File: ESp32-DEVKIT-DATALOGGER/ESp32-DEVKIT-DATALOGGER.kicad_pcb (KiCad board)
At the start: 2 copper layers, 9 parts, among them J1 Socket_01x02, J2 Conn_01x04, SW1 SW_Omron_B3FS, U1 ESP32-S3-MINI-1-N8

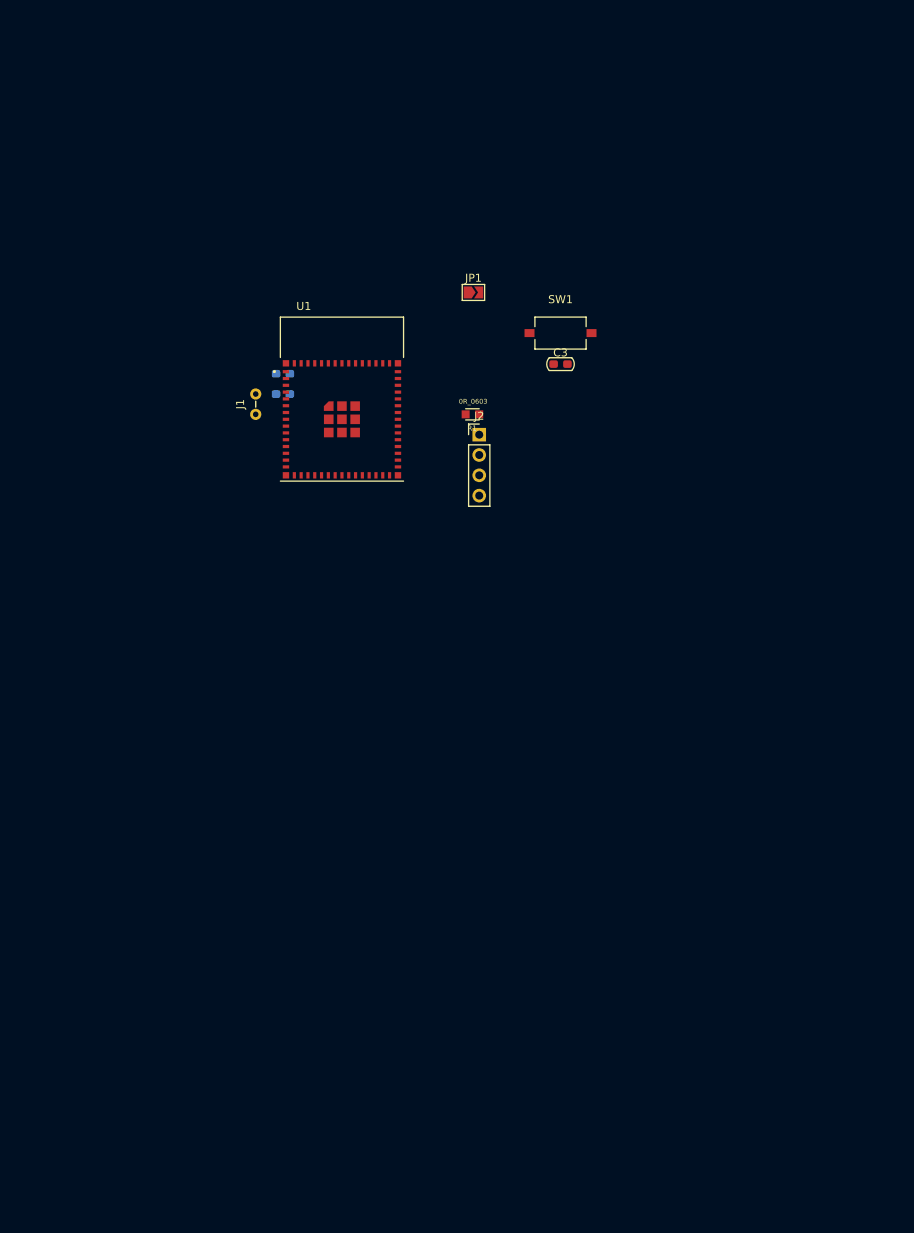
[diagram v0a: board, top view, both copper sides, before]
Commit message: Basic Structure made, need more refining and parts
Add the Filtering to the CAN and RS485, If make money this month
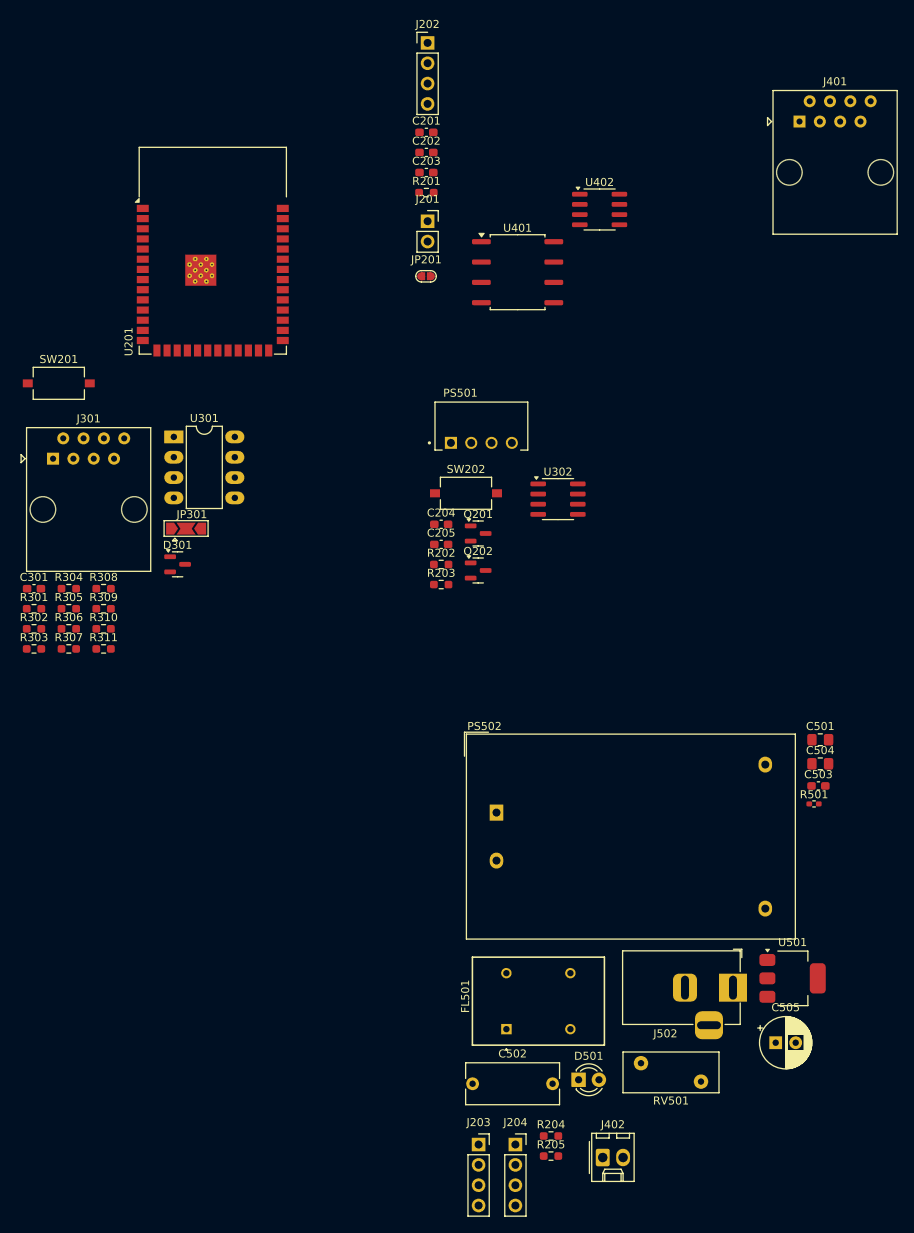
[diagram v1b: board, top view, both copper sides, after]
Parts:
- removed C1, C3: 0.1uF_0603_16V, PCM_Capacitor_SMD_AKL:C_0603_1608Metric_Pad1.08x0.95mm
- removed C2: 22uF_0603_16V, PCM_Capacitor_SMD_AKL:C_0603_1608Metric_Pad1.08x0.95mm
- removed J1: Socket_01x02, PCM_Jumper_AKL:Jumper_P2.54mm_D0.7mm
- removed J2: Conn_01x04, Connector_PinHeader_2.54mm:PinHeader_1x04_P2.54mm_Vertical
- removed JP1: SolderJumper_2_Open, Jumper:SolderJumper-2_P1.3mm_Open_TrianglePad1.0x1.5mm
- removed R1: 0R_0603, PCM_4ms_Resistor:R_0603
- removed SW1: SW_Omron_B3FS, Button_Switch_SMD:SW_Tactile_SPST_NO_Straight_CK_PTS636Sx25SMTRLFS
- removed U1: ESP32-S3-MINI-1-N8, digikey-footprints:XCVR_ESP32-S3-MINI-1-N8
- added C201: 1uF, Capacitor_SMD:C_0603_1608Metric_Pad1.08x0.95mm_HandSolder, F.Cu at (227.1, 28.2)
- added C202: 10uF, Capacitor_SMD:C_0603_1608Metric_Pad1.08x0.95mm_HandSolder, F.Cu at (227.1, 30.8)
- added C203: 100nF, Capacitor_SMD:C_0603_1608Metric_Pad1.08x0.95mm_HandSolder, F.Cu at (227.1, 33.3)
- added C204: 0.1uF, Capacitor_SMD:C_0603_1608Metric_Pad1.08x0.95mm_HandSolder, F.Cu at (228.9, 77.2)
- added C205: 100nF, Capacitor_SMD:C_0603_1608Metric_Pad1.08x0.95mm_HandSolder, F.Cu at (228.9, 79.8)
- added C301: 0.1MFD/16V, Capacitor_SMD:C_0603_1608Metric_Pad1.08x0.95mm_HandSolder, F.Cu at (178.0, 85.3)
- added C501: 10MFD/16V, Capacitor_SMD:C_0805_2012Metric_Pad1.18x1.45mm_HandSolder, F.Cu at (276.3, 104.2)
- added C502: 0.1MFD/250VAC, Capacitor_THT:C_Rect_L11.5mm_W5.0mm_P10.00mm_MKT, F.Cu at (232.8, 147.2)
- added C503: 0.1MFD/16V, Capacitor_SMD:C_0603_1608Metric_Pad1.08x0.95mm_HandSolder, F.Cu at (276.1, 109.9)
- added C504: 0.1MFD/16V, Capacitor_SMD:C_0805_2012Metric_Pad1.18x1.45mm_HandSolder, F.Cu at (276.3, 107.2)
- added C505: C_Polarized_Small_US, Capacitor_THT:CP_Radial_D6.3mm_P2.50mm, F.Cu at (270.7, 142.0)
- added D301: SM712_SOT23, Package_TO_SOT_SMD:SOT-23, F.Cu at (196.0, 82.2)
- added D501: 3mm RED, LED_THT:LED_D3.0mm, F.Cu at (246.1, 146.7)
- added FL501: 10mH, Manupa:B82730U3951A020, F.Cu at (237.1, 140.3)
- added J201: Socket_01x02, Connector_PinSocket_2.54mm:PinSocket_1x02_P2.54mm_Vertical, F.Cu at (227.2, 39.4)
- added J202: Conn_01x04, Connector_PinHeader_2.54mm:PinHeader_1x04_P2.54mm_Vertical, F.Cu at (227.2, 17.1)
- added J203: Conn_01x04_Socket, Connector_PinSocket_2.54mm:PinSocket_1x04_P2.54mm_Vertical, F.Cu at (233.6, 154.8)
- added J204: Conn_01x04_Socket, Connector_PinSocket_2.54mm:PinSocket_1x04_P2.54mm_Vertical, F.Cu at (238.2, 154.8)
- added J301: RJ45, Connector_RJ:RJ45_Amphenol_54602-x08_Horizontal, F.Cu at (180.4, 69.0)
- added J401: RJ45, Connector_RJ:RJ45_Amphenol_54602-x08_Horizontal, F.Cu at (273.7, 26.9)
- added J402: Conn_01x02_Socket, Connector_Molex:Molex_KK-254_AE-6410-02A_1x02_P2.54mm_Vertical, F.Cu at (249.1, 156.4)
- added J502: Barrel_Jack_Switch_Pin3Ring, Connector_BarrelJack:BarrelJack_Horizontal, F.Cu at (265.4, 135.2)
- added JP201: SolderJumper_2_Open, Manupa:small_jumper, F.Cu at (227.1, 46.0)
- added JP301: SolderJumper_3_Open, Jumper:SolderJumper-3_P2.0mm_Open_TrianglePad1.0x1.5mm, F.Cu at (197.0, 77.8)
- added PS501: B0505S-1WR3, B0505S-1WR3:CONV_B0505S-1WR3, F.Cu at (233.9, 65.0)
- added PS502: HLK-5M05, Converter_ACDC:Converter_ACDC_Hi-Link_HLK-5Mxx, F.Cu at (235.8, 113.3)
- added Q201: MMBT3904, Package_TO_SOT_SMD:SOT-23, F.Cu at (233.5, 78.4)
- added Q202: MMBT3904, Package_TO_SOT_SMD:SOT-23, F.Cu at (233.5, 83.0)
- added R201: 0R_0603, Resistor_SMD:R_0603_1608Metric_Pad0.98x0.95mm_HandSolder, F.Cu at (227.1, 35.8)
- added R202: 0R_0603, Resistor_SMD:R_0603_1608Metric_Pad0.98x0.95mm_HandSolder, F.Cu at (228.9, 82.3)
- added R203: 0R_0603, Resistor_SMD:R_0603_1608Metric_Pad0.98x0.95mm_HandSolder, F.Cu at (228.9, 84.8)
- added R204: 0R_0603, Resistor_SMD:R_0603_1608Metric_Pad0.98x0.95mm_HandSolder, F.Cu at (242.7, 153.7)
- added R205: 0R_0603, Resistor_SMD:R_0603_1608Metric_Pad0.98x0.95mm_HandSolder, F.Cu at (242.7, 156.2)
- added R301: 10K, Resistor_SMD:R_0603_1608Metric_Pad0.98x0.95mm_HandSolder, F.Cu at (178.0, 87.8)
- added R302: 10K, Resistor_SMD:R_0603_1608Metric_Pad0.98x0.95mm_HandSolder, F.Cu at (178.0, 90.3)
- added R303: 10K, Resistor_SMD:R_0603_1608Metric_Pad0.98x0.95mm_HandSolder, F.Cu at (178.0, 92.8)
- added R304: 10K, Resistor_SMD:R_0603_1608Metric_Pad0.98x0.95mm_HandSolder, F.Cu at (182.4, 85.3)
- added R305: 10K, Resistor_SMD:R_0603_1608Metric_Pad0.98x0.95mm_HandSolder, F.Cu at (182.4, 87.8)
- added R306: 120R, Resistor_SMD:R_0603_1608Metric_Pad0.98x0.95mm_HandSolder, F.Cu at (182.4, 90.3)
- added R307: 10K, Resistor_SMD:R_0603_1608Metric_Pad0.98x0.95mm_HandSolder, F.Cu at (182.4, 92.8)
- added R308: 10K, Resistor_SMD:R_0603_1608Metric_Pad0.98x0.95mm_HandSolder, F.Cu at (186.7, 85.3)
- added R309: 10K, Resistor_SMD:R_0603_1608Metric_Pad0.98x0.95mm_HandSolder, F.Cu at (186.7, 87.8)
- added R310: 10K, Resistor_SMD:R_0603_1608Metric_Pad0.98x0.95mm_HandSolder, F.Cu at (186.7, 90.3)
- added R311: 10K, Resistor_SMD:R_0603_1608Metric_Pad0.98x0.95mm_HandSolder, F.Cu at (186.7, 92.8)
- added R501: 1.5K, Resistor_SMD:R_0402_1005Metric_Pad0.72x0.64mm_HandSolder, F.Cu at (275.5, 112.2)
- added RV501: 10D561, Varistor:RV_Disc_D12mm_W5.1mm_P7.5mm, F.Cu at (253.9, 144.6)
- added SW201: SW_Omron_B3FS, Button_Switch_SMD:SW_Tactile_SPST_NO_Straight_CK_PTS636Sx25SMTRLFS, F.Cu at (181.1, 59.6)
- added SW202: SW_Omron_B3FS, Button_Switch_SMD:SW_Tactile_SPST_NO_Straight_CK_PTS636Sx25SMTRLFS, F.Cu at (232.0, 73.4)
- added U201: ESP32-S3-WROOM-1, RF_Module:ESP32-S3-WROOM-1, F.Cu at (200.4, 43.0)
- added U301: MAX485E, Package_DIP:DIP-8_W7.62mm_LongPads, F.Cu at (195.5, 66.3)
- added U302: MAX3486, Package_SO:SOIC-8_3.9x4.9mm_P1.27mm, F.Cu at (243.5, 74.1)
- added U401: ISO1050DUB, Package_SO:SOP-8_6.62x9.15mm_P2.54mm, F.Cu at (238.5, 45.7)
- added U402: TJA1051T, Package_SO:SOIC-8_3.9x4.9mm_P1.27mm, F.Cu at (248.7, 37.9)
- added U501: AMS1117-3.3, Package_TO_SOT_SMD:SOT-223-3_TabPin2, F.Cu at (272.9, 134.0)

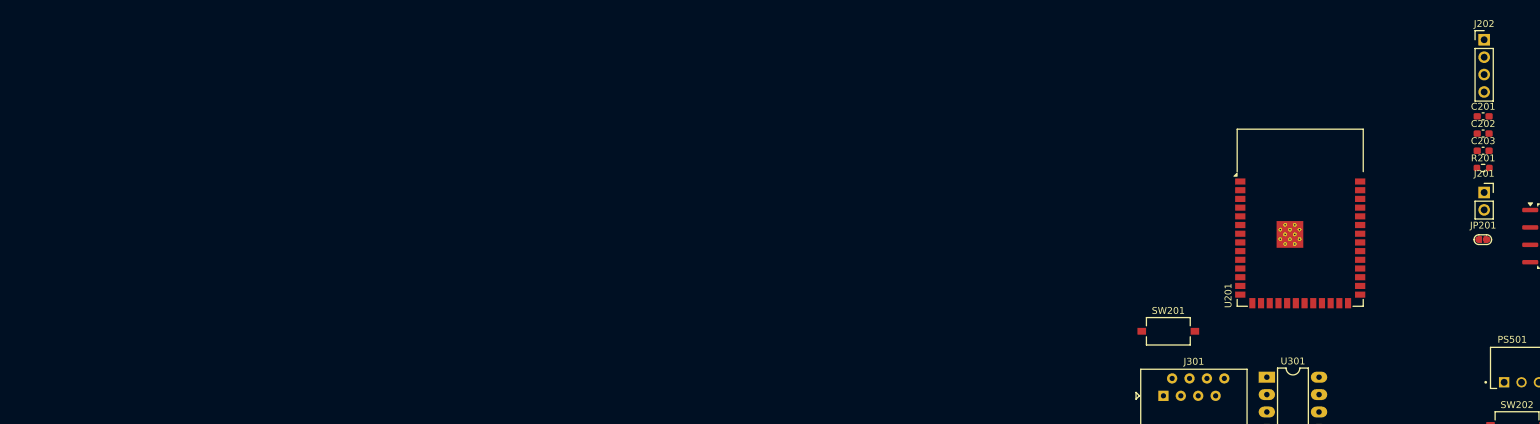
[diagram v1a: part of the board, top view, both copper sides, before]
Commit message: Small Changes
Adding I2C components
More RS485
And it is required changing the  Labels for RS485 . for 3 different channels
And Make them ISO Pins
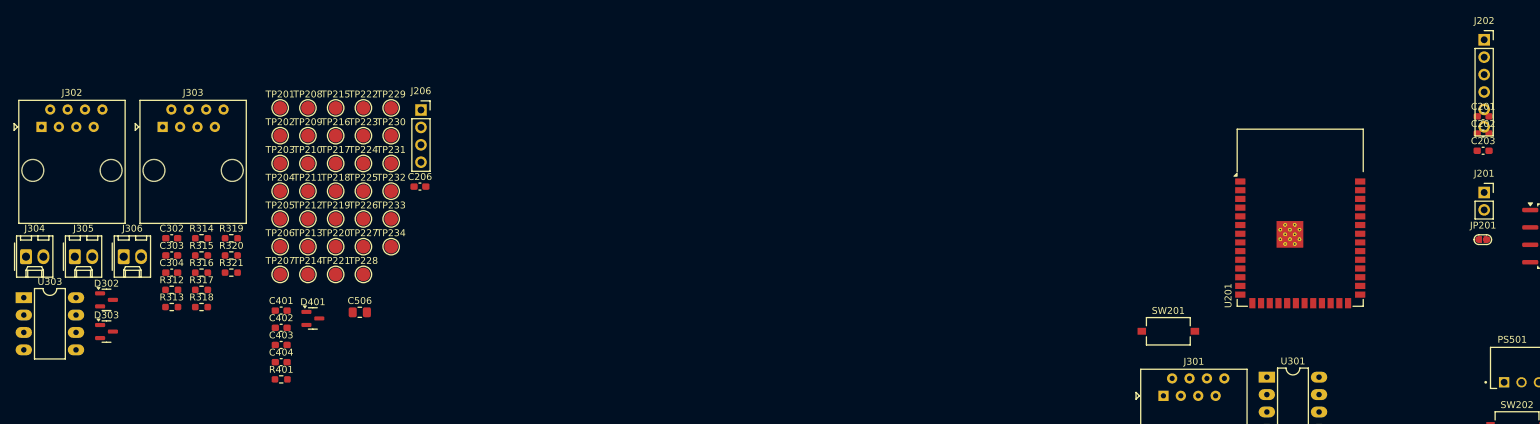
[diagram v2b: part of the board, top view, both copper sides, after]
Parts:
- removed R201: 0R_0603, Resistor_SMD:R_0603_1608Metric_Pad0.98x0.95mm_HandSolder
- added C206: 100nF, Capacitor_SMD:C_0603_1608Metric_Pad1.08x0.95mm_HandSolder, F.Cu at (71.9, 38.5)
- added C302: 0.1MFD/16V, Capacitor_SMD:C_0603_1608Metric_Pad1.08x0.95mm_HandSolder, F.Cu at (35.7, 46.0)
- added C303: 0.1MFD/16V, Capacitor_SMD:C_0603_1608Metric_Pad1.08x0.95mm_HandSolder, F.Cu at (35.7, 48.5)
- added C304: 0.1MFD/16V, Capacitor_SMD:C_0603_1608Metric_Pad1.08x0.95mm_HandSolder, F.Cu at (35.7, 51.1)
- added C401: 100nF, Capacitor_SMD:C_0603_1608Metric_Pad1.08x0.95mm_HandSolder, F.Cu at (51.6, 56.6)
- added C402: 100nF, Capacitor_SMD:C_0603_1608Metric_Pad1.08x0.95mm_HandSolder, F.Cu at (51.6, 59.1)
- added C403: 100nF, Capacitor_SMD:C_0603_1608Metric_Pad1.08x0.95mm_HandSolder, F.Cu at (51.6, 61.6)
- added C404: 100nF, Capacitor_SMD:C_0603_1608Metric_Pad1.08x0.95mm_HandSolder, F.Cu at (51.6, 64.1)
- added C506: 0.1MFD/16V, Capacitor_SMD:C_0805_2012Metric_Pad1.18x1.45mm_HandSolder, F.Cu at (63.1, 56.9)
- added D302: SM712_SOT23, Package_TO_SOT_SMD:SOT-23, F.Cu at (26.1, 55.0)
- added D303: SM712_SOT23, Package_TO_SOT_SMD:SOT-23, F.Cu at (26.1, 59.7)
- added D401: SM712_SOT23, Package_TO_SOT_SMD:SOT-23, F.Cu at (56.3, 57.7)
- added J206: Conn_01x04_Socket, Connector_PinSocket_2.54mm:PinSocket_1x04_P2.54mm_Vertical, F.Cu at (72.0, 27.3)
- added J302: RJ45, Connector_RJ:RJ45_Amphenol_54602-x08_Horizontal, F.Cu at (16.7, 29.8)
- added J303: RJ45, Connector_RJ:RJ45_Amphenol_54602-x08_Horizontal, F.Cu at (34.3, 29.8)
- added J304: Conn_01x02_Socket, Connector_Molex:Molex_KK-254_AE-6410-02A_1x02_P2.54mm_Vertical, F.Cu at (14.4, 48.7)
- added J305: Conn_01x02_Socket, Connector_Molex:Molex_KK-254_AE-6410-02A_1x02_P2.54mm_Vertical, F.Cu at (21.5, 48.7)
- added J306: Conn_01x02_Socket, Connector_Molex:Molex_KK-254_AE-6410-02A_1x02_P2.54mm_Vertical, F.Cu at (28.6, 48.7)
- added R312: 10K, Resistor_SMD:R_0603_1608Metric_Pad0.98x0.95mm_HandSolder, F.Cu at (35.7, 53.6)
- added R313: 10K, Resistor_SMD:R_0603_1608Metric_Pad0.98x0.95mm_HandSolder, F.Cu at (35.7, 56.1)
- added R314: 10K, Resistor_SMD:R_0603_1608Metric_Pad0.98x0.95mm_HandSolder, F.Cu at (40.0, 46.0)
- added R315: 10K, Resistor_SMD:R_0603_1608Metric_Pad0.98x0.95mm_HandSolder, F.Cu at (40.0, 48.5)
- added R316: 10K, Resistor_SMD:R_0603_1608Metric_Pad0.98x0.95mm_HandSolder, F.Cu at (40.0, 51.1)
- added R317: 10K, Resistor_SMD:R_0603_1608Metric_Pad0.98x0.95mm_HandSolder, F.Cu at (40.0, 53.6)
- added R318: 120R, Resistor_SMD:R_0603_1608Metric_Pad0.98x0.95mm_HandSolder, F.Cu at (40.0, 56.1)
- added R319: 10K, Resistor_SMD:R_0603_1608Metric_Pad0.98x0.95mm_HandSolder, F.Cu at (44.4, 46.0)
- added R320: 10K, Resistor_SMD:R_0603_1608Metric_Pad0.98x0.95mm_HandSolder, F.Cu at (44.4, 48.5)
- added R321: 120R, Resistor_SMD:R_0603_1608Metric_Pad0.98x0.95mm_HandSolder, F.Cu at (44.4, 51.1)
- added R401: 120R, Resistor_SMD:R_0603_1608Metric_Pad0.98x0.95mm_HandSolder, F.Cu at (51.6, 66.6)
- added TP201: TestPoint, TestPoint:TestPoint_Pad_D2.0mm, F.Cu at (51.5, 27.0)
- added TP202: TestPoint, TestPoint:TestPoint_Pad_D2.0mm, F.Cu at (51.5, 31.1)
- added TP203: TestPoint, TestPoint:TestPoint_Pad_D2.0mm, F.Cu at (51.5, 35.1)
- added TP204: TestPoint, TestPoint:TestPoint_Pad_D2.0mm, F.Cu at (51.5, 39.2)
- added TP205: TestPoint, TestPoint:TestPoint_Pad_D2.0mm, F.Cu at (51.5, 43.2)
- added TP206: TestPoint, TestPoint:TestPoint_Pad_D2.0mm, F.Cu at (51.5, 47.3)
- added TP207: TestPoint, TestPoint:TestPoint_Pad_D2.0mm, F.Cu at (51.5, 51.3)
- added TP208: TestPoint, TestPoint:TestPoint_Pad_D2.0mm, F.Cu at (55.5, 27.0)
- added TP209: TestPoint, TestPoint:TestPoint_Pad_D2.0mm, F.Cu at (55.5, 31.1)
- added TP210: TestPoint, TestPoint:TestPoint_Pad_D2.0mm, F.Cu at (55.5, 35.1)
- added TP211: TestPoint, TestPoint:TestPoint_Pad_D2.0mm, F.Cu at (55.5, 39.2)
- added TP212: TestPoint, TestPoint:TestPoint_Pad_D2.0mm, F.Cu at (55.5, 43.2)
- added TP213: TestPoint, TestPoint:TestPoint_Pad_D2.0mm, F.Cu at (55.5, 47.3)
- added TP214: TestPoint, TestPoint:TestPoint_Pad_D2.0mm, F.Cu at (55.5, 51.3)
- added TP215: TestPoint, TestPoint:TestPoint_Pad_D2.0mm, F.Cu at (59.6, 27.0)
- added TP216: TestPoint, TestPoint:TestPoint_Pad_D2.0mm, F.Cu at (59.6, 31.1)
- added TP217: TestPoint, TestPoint:TestPoint_Pad_D2.0mm, F.Cu at (59.6, 35.1)
- added TP218: TestPoint, TestPoint:TestPoint_Pad_D2.0mm, F.Cu at (59.6, 39.2)
- added TP219: TestPoint, TestPoint:TestPoint_Pad_D2.0mm, F.Cu at (59.6, 43.2)
- added TP220: TestPoint, TestPoint:TestPoint_Pad_D2.0mm, F.Cu at (59.6, 47.3)
- added TP221: TestPoint, TestPoint:TestPoint_Pad_D2.0mm, F.Cu at (59.6, 51.3)
- added TP222: TestPoint, TestPoint:TestPoint_Pad_D2.0mm, F.Cu at (63.6, 27.0)
- added TP223: TestPoint, TestPoint:TestPoint_Pad_D2.0mm, F.Cu at (63.6, 31.1)
- added TP224: TestPoint, TestPoint:TestPoint_Pad_D2.0mm, F.Cu at (63.6, 35.1)
- added TP225: TestPoint, TestPoint:TestPoint_Pad_D2.0mm, F.Cu at (63.6, 39.2)
- added TP226: TestPoint, TestPoint:TestPoint_Pad_D2.0mm, F.Cu at (63.6, 43.2)
- added TP227: TestPoint, TestPoint:TestPoint_Pad_D2.0mm, F.Cu at (63.6, 47.3)
- added TP228: TestPoint, TestPoint:TestPoint_Pad_D2.0mm, F.Cu at (63.6, 51.3)
- added TP229: TestPoint, TestPoint:TestPoint_Pad_D2.0mm, F.Cu at (67.7, 27.0)
- added TP230: TestPoint, TestPoint:TestPoint_Pad_D2.0mm, F.Cu at (67.7, 31.1)
- added TP231: TestPoint, TestPoint:TestPoint_Pad_D2.0mm, F.Cu at (67.7, 35.1)
- added TP232: TestPoint, TestPoint:TestPoint_Pad_D2.0mm, F.Cu at (67.7, 39.2)
- added TP233: TestPoint, TestPoint:TestPoint_Pad_D2.0mm, F.Cu at (67.7, 43.2)
- added TP234: TestPoint, TestPoint:TestPoint_Pad_D2.0mm, F.Cu at (67.7, 47.3)
- added U303: MAX485E, Package_DIP:DIP-8_W7.62mm_LongPads, F.Cu at (14.1, 54.7)
- J202: value Conn_01x04 -> Conn_01x06_Socket; footprint Connector_PinHeader_2.54mm:PinHeader_1x04_P2.54mm_Vertical -> Connector_PinSocket_2.54mm:PinSocket_1x06_P2.54mm_Vertical
- R306: value 120R -> 10K
- R307: value 10K -> 120R
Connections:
- C301 pad 1: +5V -> RS485_VCC
- D301 pad 1: A -> A2
- D301 pad 2: B -> B2
- J202 pad 1: VCC -> /esp32-module/DTR
- J202 pad 2: UART0RX -> UART0TX
- J202 pad 3: UART0TX -> UART0RX
- J202 pad 4: GND -> VCC
- J301 pad 1: B -> B1
- J301 pad 2: A -> A1
- J301 pad 7: A -> A1
- J301 pad 8: B -> B1
- JP301 pad 2: Net-(JP301-C) -> RS485_VCC
- R301 pad 2: 3V3 -> RS485_VCC
- R302 pad 2: 3V3 -> RS485_VCC
- R303 pad 2: 3V3 -> RS485_VCC
- R304 pad 2: 3V3 -> RS485_VCC
- R305 pad 1: A -> A2
- R305 pad 2: Net-(JP301-C) -> RS485_VCC
- R306 pad 1: A -> B2
- R306 pad 2: B -> GND
- R307 pad 1: B -> A2
- R307 pad 2: GND -> B2
- R308 pad 2: +5V -> RS485_VCC
- R309 pad 2: +5V -> RS485_VCC
- R310 pad 2: +5V -> RS485_VCC
- R311 pad 2: +5V -> RS485_VCC
- U201 pad 12: unconnected-(U201-IO8-Pad12) -> IO8
- U201 pad 13: unconnected-(U201-IO19-Pad13) -> USB +
- U201 pad 14: unconnected-(U201-IO20-Pad14) -> USB -
- U201 pad 15: unconnected-(U201-IO3-Pad15) -> IO3
- U201 pad 16: unconnected-(U201-IO46-Pad16) -> IO46
- U201 pad 17: unconnected-(U201-IO9-Pad17) -> IO9
- U201 pad 18: unconnected-(U201-IO10-Pad18) -> IO10
- U201 pad 19: unconnected-(U201-IO11-Pad19) -> IO11
- U201 pad 20: unconnected-(U201-IO12-Pad20) -> IO12
- U201 pad 21: unconnected-(U201-IO13-Pad21) -> IO13
- U201 pad 22: unconnected-(U201-IO14-Pad22) -> IO14
- U201 pad 23: unconnected-(U201-IO21-Pad23) -> /esp32-module/MISO
- U201 pad 24: unconnected-(U201-IO47-Pad24) -> SCL
- U201 pad 25: unconnected-(U201-IO48-Pad25) -> SDA
- U201 pad 26: unconnected-(U201-IO45-Pad26) -> /esp32-module/SD_CS
- U201 pad 31: unconnected-(U201-IO38-Pad31) -> IO38
- U201 pad 32: unconnected-(U201-IO39-Pad32) -> /esp32-module/SCK
- U201 pad 33: unconnected-(U201-IO40-Pad33) -> IO40
- U201 pad 34: unconnected-(U201-IO41-Pad34) -> IO41
- U201 pad 35: unconnected-(U201-IO42-Pad35) -> /esp32-module/MOSI
- U201 pad 38: unconnected-(U201-IO2-Pad38) -> IO2
- U201 pad 39: unconnected-(U201-IO1-Pad39) -> IO1
- U201 pad 4: SCL -> IO4
- U201 pad 5: SDA -> IO5
- U201 pad 6: unconnected-(U201-IO6-Pad6) -> IO6
- U201 pad 7: unconnected-(U201-IO7-Pad7) -> IO7
- U201 pad 8: unconnected-(U201-IO15-Pad8) -> IO15
- U201 pad 9: unconnected-(U201-IO16-Pad9) -> IO16
- U301 pad 6: A -> A2
- U301 pad 7: B -> B2
- U301 pad 8: +5V -> RS485_VCC
- U302 pad 6: A -> A1
- U302 pad 7: B -> B1
- U302 pad 8: 3V3 -> RS485_VCC
